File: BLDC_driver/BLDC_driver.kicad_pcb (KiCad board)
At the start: 4 copper layers, 100 x 100 mm, 125 parts, among them J1 CTRL, J2 POWER, J3 JTAG, J4 USB-C 16P, Q1 AOTL66912, Q10 AOTL66912, Q11 AOTL66912, Q12 AOTL66912, Q13 AOTL66912, Q14 AOTL66912, Q15 AOTL66912, Q16 AOTL66912, Q17 AOTL66912, Q18 AOTL66912, Q2 AOTL66912, Q3 AOTL66912, Q4 AOTL66912, Q5 AOTL66912, Q6 AOTL66912, Q7 AOTL66912, Q8 AOTL66912, Q9 AOTL66912, SW1 BTN, SW2 BTN, U1 STM32F412CEUx, U2 W25Q128JVS, U3 USBLC6-2SC6, Y1 25MHz

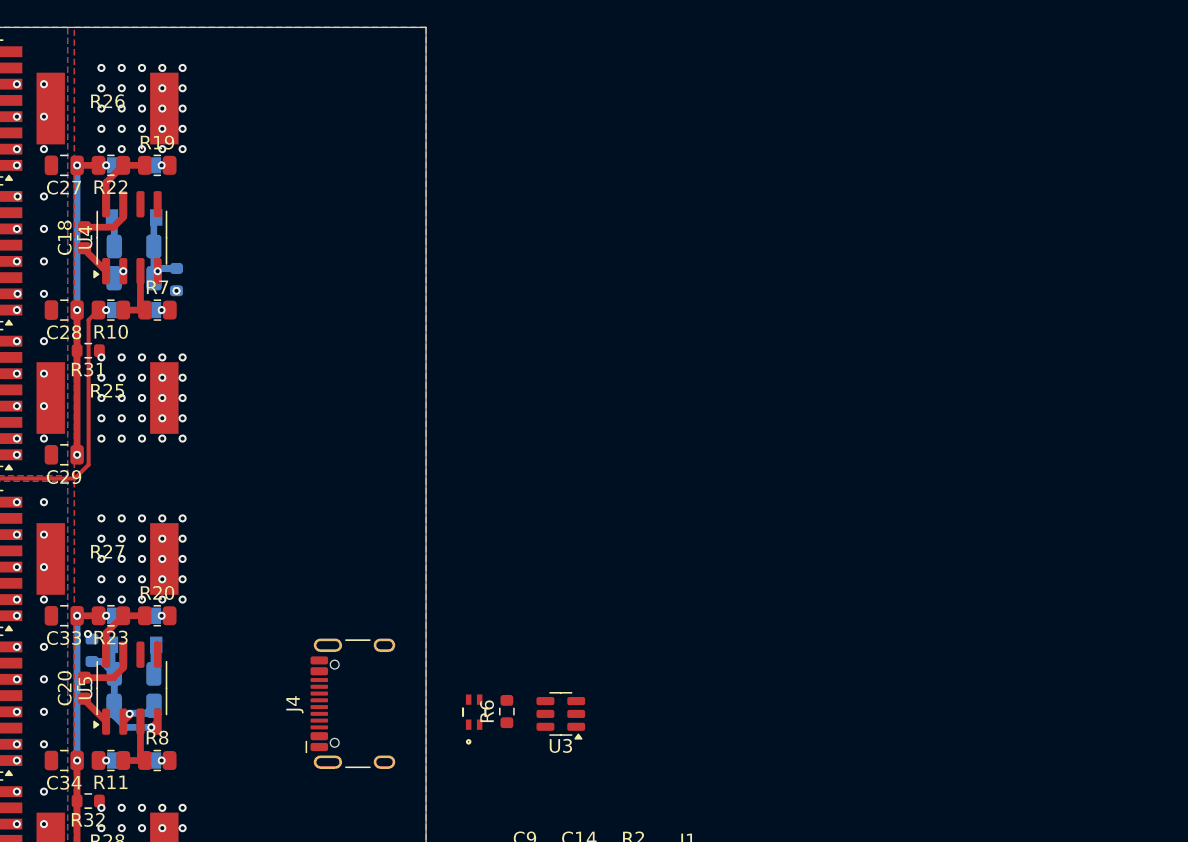
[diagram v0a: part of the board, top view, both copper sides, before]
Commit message: Started on power conversion section
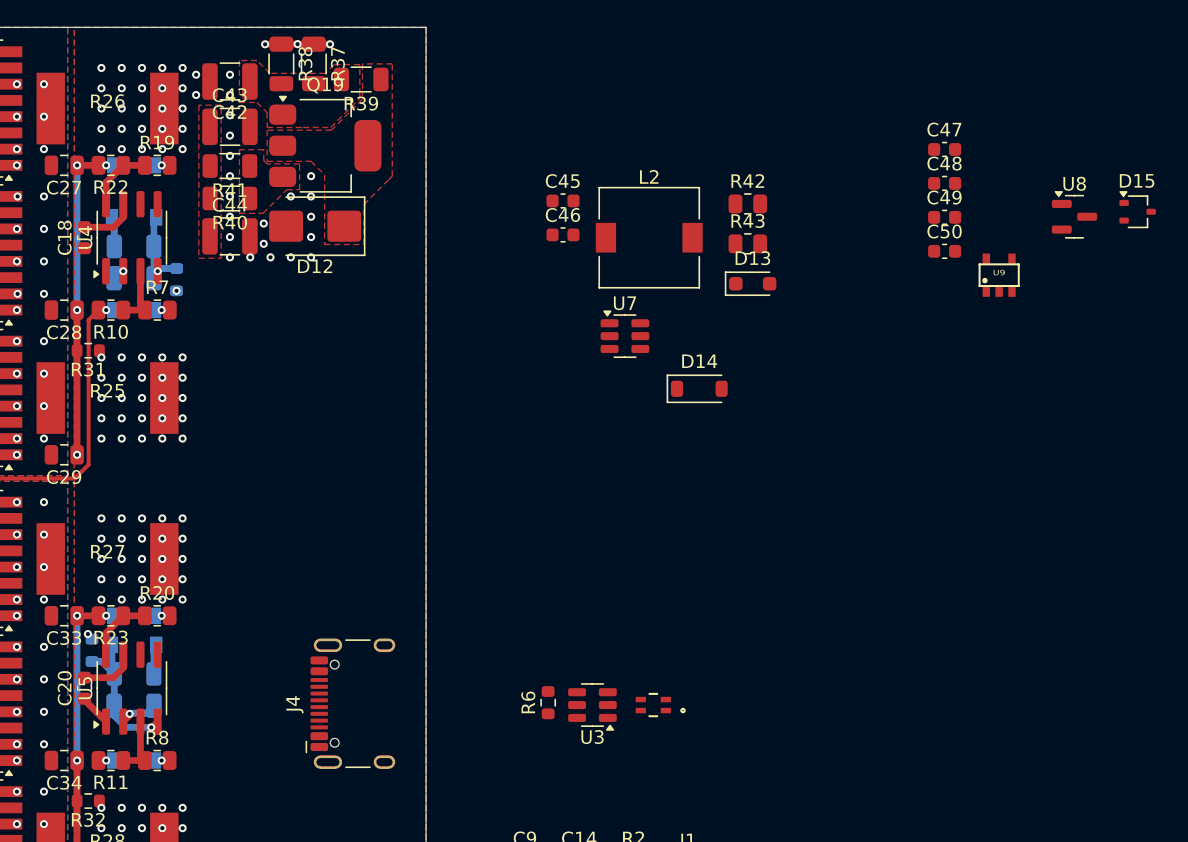
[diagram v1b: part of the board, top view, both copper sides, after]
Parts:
- added C42: 2u2/100v, Capacitor_SMD:C_1210_3225Metric, F.Cu at (152.0, 66.0)
- added C43: 4u7/100v, Capacitor_SMD:C_1210_3225Metric, F.Cu at (152.0, 69.4)
- added C44: 4u7/100v, Capacitor_SMD:C_1210_3225Metric, F.Cu at (152.0, 77.5)
- added C45: 100n, Capacitor_SMD:C_0603_1608Metric, F.Cu at (176.6, 74.8)
- added C46: 22u, Capacitor_SMD:C_0603_1608Metric, F.Cu at (176.6, 77.4)
- added C47: 1u, Capacitor_SMD:C_0603_1608Metric, F.Cu at (204.8, 71.0)
- added C48: 4u7, Capacitor_SMD:C_0603_1608Metric, F.Cu at (204.8, 73.6)
- added C49: 1u, Capacitor_SMD:C_0603_1608Metric, F.Cu at (204.8, 76.1)
- added C50: 1u, Capacitor_SMD:C_0603_1608Metric, F.Cu at (204.8, 78.6)
- added D12: BZG03C43-HM3-08, Diode_SMD:D_SMB, F.Cu at (158.3, 76.7)
- added D13: 1N4148WS, Diode_SMD:D_SOD-323_HandSoldering, F.Cu at (190.6, 81.0)
- added D14: MMSZ7V5T1G, Diode_SMD:D_SOD-123, F.Cu at (186.7, 88.7)
- added D15: BAT54AW, Package_TO_SOT_SMD:SOT-323_SC-70, F.Cu at (219.1, 75.7)
- added L2: 56u, Inductor_SMD:L_7.3x7.3_H4.5, F.Cu at (183.0, 77.6)
- added Q19: FZT853TA, Package_TO_SOT_SMD:SOT-223-3_TabPin2, F.Cu at (159.0, 70.8)
- added R37: 3r3, Resistor_SMD:R_1206_3216Metric, F.Cu at (158.2, 64.7)
- added R38: 3r3, Resistor_SMD:R_1206_3216Metric, F.Cu at (155.8, 64.7)
- added R39: 2k2, Resistor_SMD:R_1206_3216Metric, F.Cu at (161.7, 65.9)
- added R40: 3r3, Resistor_SMD:R_1206_3216Metric, F.Cu at (152.0, 74.7)
- added R41: 3r3, Resistor_SMD:R_1206_3216Metric, F.Cu at (152.0, 72.3)
- added R42: 140k, Resistor_SMD:R_0805_2012Metric, F.Cu at (190.3, 75.1)
- added R43: 10k, Resistor_SMD:R_0805_2012Metric, F.Cu at (190.3, 78.0)
- added U7: MCP16331x-xCH, Package_TO_SOT_SMD:SOT-23-6, F.Cu at (181.2, 84.8)
- added U8: MCP1754S-3302xCB, Package_TO_SOT_SMD:SOT-23, F.Cu at (214.4, 76.0)
- added U9: ~, Custom:SOT-25, F.Cu at (208.9, 80.3)
- moved FL1 13.3 mm to (183.3, 112.1), turned to 180 degrees
- moved R6 3.12 mm to (175.5, 111.9)
- moved U3 2.43 mm to (178.8, 112.1)
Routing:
- net VPWR: track 0.00 -> 4.81 mm, vias 0 -> 3
- net +12V: track 7.08 -> 4.72 mm
- net GND: vias 150 -> 173
- added copper zone on F.Cu, net +43V
- added copper zone on F.Cu, net Net-(D12-K)
- added copper zone on F.Cu, net Net-(Q19-C)
- added copper zone on F.Cu, net Net-(Q19-E)

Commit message: Power converter layout
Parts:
- D15: value BAT54AW -> BAT54C; footprint Package_TO_SOT_SMD:SOT-323_SC-70 -> Package_TO_SOT_SMD:SOT-23
- FL1, U3: moved to B.Cu
- U9: value ~ -> AP7343; footprint Custom:SOT-25 -> Marijn_KiCad:SOT-25
- moved D15 65.8 mm to (155.5, 92.9), turned to 180 degrees
- moved U8 55.8 mm to (160.9, 91.6), turned to -90 degrees
- moved U9 50.3 mm to (160.9, 95.4), turned to 90 degrees
- moved C48 49.9 mm to (158.4, 91.6), turned to -90 degrees
- moved C50 49.4 mm to (158.3, 95.4), turned to 90 degrees
- moved C47 46.2 mm to (163.4, 91.6), turned to 90 degrees
- moved C49 45.7 mm to (163.4, 95.4), turned to 90 degrees
- moved R43 35.5 mm to (154.8, 80.9), turned to 90 degrees
- moved R42 34.0 mm to (156.8, 80.9), turned to -90 degrees
- moved D13 31.5 mm to (159.6, 86.0)
- moved L2 30.8 mm to (153.6, 86.9), turned to 90 degrees
- moved U7 29.7 mm to (151.7, 80.9), turned to 180 degrees
- moved D14 27.2 mm to (159.9, 83.8)
- moved FL1 26.3 mm to (157.0, 112.0), turned to 0 degrees
- moved C45 22.9 mm to (158.3, 88.6), turned to -90 degrees
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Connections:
- net /power/a renamed Net-(U7-V_{FB})
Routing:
- net +12V: track 4.72 -> 115.3 mm, vias 0 -> 4
- net +5V: track 0.00 -> 29.2 mm, vias 0 -> 1
- net Net-(U7-SW): track 0.00 -> 14.5 mm
- net GND: track 18.9 -> 32.4 mm, vias 173 -> 206
- net Net-(D13-K): track 0.00 -> 12.3 mm
- net Net-(J4-CC1): track 0.00 -> 5.74 mm
- net /USB/FL_P: track 0.00 -> 5.66 mm
- net /USB/FL_N: track 0.00 -> 5.66 mm
- net +43V: track 0.00 -> 4.69 mm
- net Net-(J4-D--PadA7): track 0.00 -> 4.53 mm, vias 0 -> 1
- net Net-(U9-VOUT): track 0.00 -> 4.52 mm
- net Net-(U8-VO): track 0.00 -> 3.98 mm
- net Net-(J4-D+-PadA6): track 0.00 -> 3.77 mm, vias 0 -> 1
- net Net-(D13-A): track 0.00 -> 2.51 mm
- net +3V3: vias 0 -> 10
- added copper zone on F.Cu, net +12V
- added copper zone on F.Cu, net +3V3
- added copper zone on F.Cu, net Net-(U7-V_{FB})
